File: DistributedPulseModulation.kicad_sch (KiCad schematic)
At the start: 59 parts, among them J1 Conn_02x12_Odd_Even, J2 Conn_01x01, U1 74LS251, U10 4053, U11 4053, U12 4053, U2 74LVC2G74, U25 74LS85, U28 74LS85, U31 74LS85, U4 MCP23017_SP, U7 4053, U8 4040, U9 4040

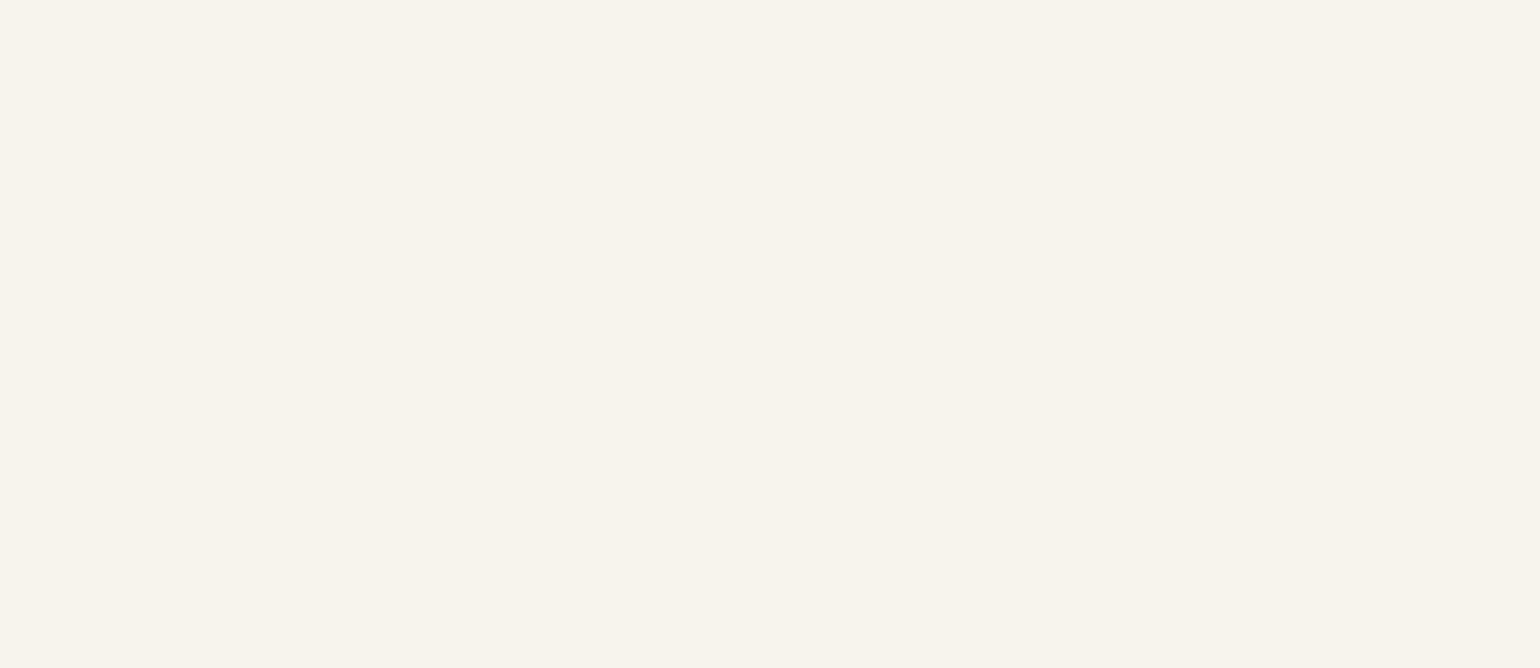
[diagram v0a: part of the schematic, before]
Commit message: [UPGRADE] : KiCad10 + Voltage -> KICAD 10 -> CMOS vs TTL voltage compare
[TODO]
-> adding replacement circuit for Dlatch chip
-> correction voltage bugs
-> remove supply voltage regulator from PCB
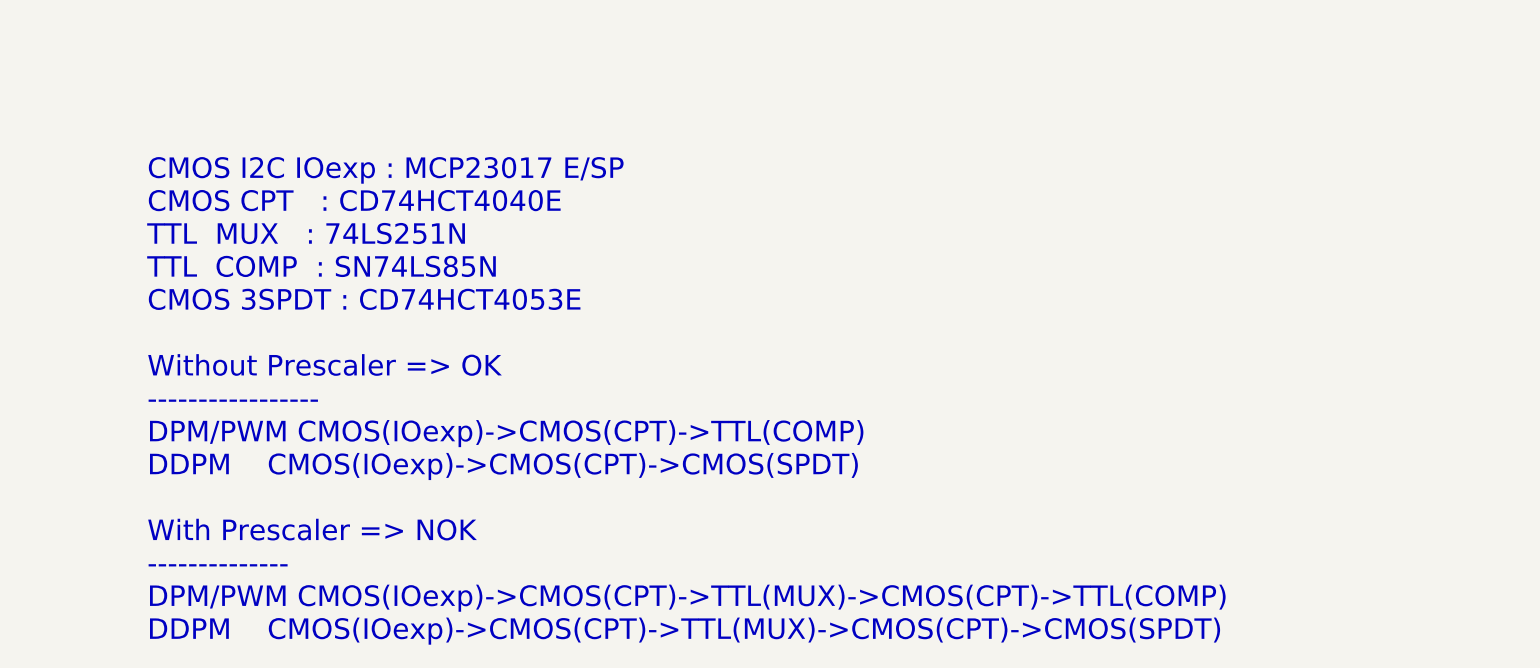
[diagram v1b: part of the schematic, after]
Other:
- note added: "CMOS I2C IOexp : MCP23017 E/SP CMOS CPT : CD74HCT4040E TTL MUX : 74LS251N TTL COMP : SN74LS85N CMOS 3SPDT : CD74HCT4053E Without Prescaler => OK ----------------- DPM/PWM CMOS(IOexp)->CMOS(CPT)->TTL(COMP) DDPM CMOS(IOexp)->CMOS(CPT)->CMOS(SPDT) With Prescaler => NOK -------------- DPM/PWM CMOS(IOexp)->CMOS(CPT)->TTL(MUX)->CMOS(CPT)->TTL(COMP) DDPM CMOS(IOexp)->CMOS(CPT)->TTL(MUX)->CMOS(CPT)->CMOS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"

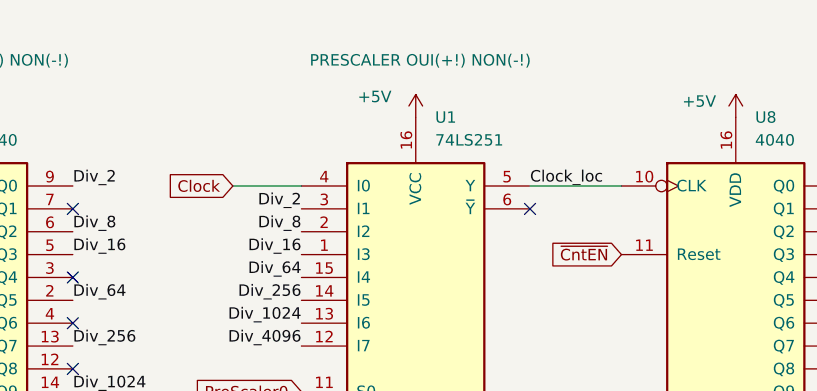
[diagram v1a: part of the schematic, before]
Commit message: [UPGRADE] : ajout R6 pour pb tension entre TTL et CMOS - A jout de R6 (2.2K) en pull-uup sur la pin 5 du 74ls251 (TTL) en entrée du 74HCT4040 (CMOS)
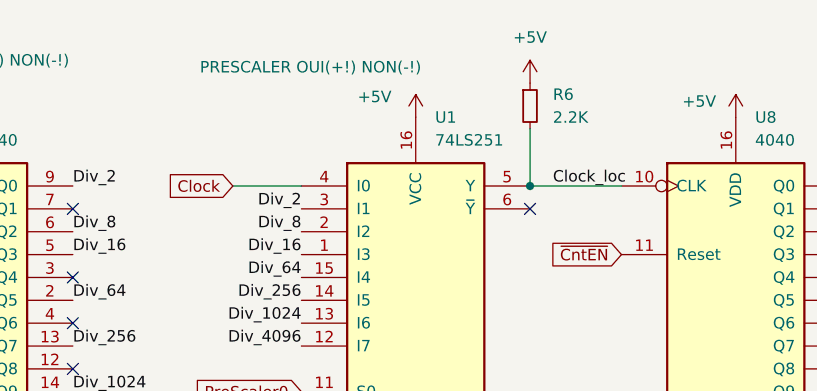
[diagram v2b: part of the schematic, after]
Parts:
- added R6: 2.2K, Resistor_SMD:R_1206_3216Metric_Pad1.30x1.75mm_HandSolder, symbol Device:R_Small
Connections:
- net +5V: now also R6.1
- net Clock_loc: now also R6.2
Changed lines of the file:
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@@
 	)
 	(junction
+		(at 105.41 36.83)
+		(diameter 0)
+		(color 0 0 0 0)
+	)
+	(junction
 		(at 212.09 260.35)
 		(diameter 0)
@@
 	(wire
 		(pts
+			(xy 105.41 30.48) (xy 105.41 36.83)
+		)
+		(stroke
+			(width 0)
+			(type default)
+		)
+	)
+	(wire
+		(pts
 			(xy 59.69 172.72) (xy 57.15 172.72)
 		)
@@
 	)
 	(label "Clock_loc"
-		(at 105.41 36.83 0)
+		(at 107.95 36.83 0)
 		(effects
 			(font
@@
 		)
 		(property "Var" "PRESCALER OUI(+!) NON(-!)"
-			(at 93.218 22.86 0)
+			(at 81.026 23.622 0)
 			(show_name no)
 			(do_not_autoplace no)
@@
 	)
 	(symbol
+		(lib_id "power:+5V")
+		(at 105.41 25.4 0)
+		(unit 1)
+		(body_style 1)
+		(exclude_from_sim no)
+		(in_bom yes)
+		(on_board yes)
+		(in_pos_files yes)
+		(dnp no)
+		(fields_autoplaced yes)
+		(property "Reference" "#PWR08"
+			(at 105.41 29.21 0)
+			(hide yes)
+			(show_name no)
+			(do_not_autoplace no)
+			(effects
+				(font
+					(size 1.27 1.27)
+				)
+			)
+		)
+		(property "Value" "+5V"
+			(at 105.41 20.32 0)
+			(show_name no)
+			(do_not_autoplace no)
+			(effects
+				(font
+					(size 1.27 1.27)
+				)
+			)
+		)
+		(property "Footprint" ""
+			(at 105.41 25.4 0)
+			(hide yes)
+			(show_name no)
+			(do_not_autoplace no)
+			(effects
+				(font
+					(size 1.27 1.27)
+				)
+			)
+		)
+		(property "Datasheet" ""
+			(at 105.41 25.4 0)
+			(hide yes)
+			(show_name no)
+			(do_not_autoplace no)
+			(effects
+				(font
+					(size 1.27 1.27)
+				)
+			)
+		)
+		(property "Description" "Power symbol creates a global label with name \"+5V\""
+			(at 105.41 25.4 0)
+			(hide yes)
+			(show_name no)
+			(do_not_autoplace no)
+			(effects
+				(font
+					(size 1.27 1.27)
+				)
+			)
+		)
+		(pin "1"
+		)
+		(instances
+			(project "DistributedPulseModulation"
+				(path "/92d35ba6-f947-4e80-8ed2-a00ad88d5264"
+					(reference "#PWR08")
+					(unit 1)
+				)
+			)
+		)
+	)
+	(symbol
 		(lib_id "74xx:74LS85")
 		(at 271.78 78.74 0)
@@
 					(unit 1)
 				)
+			)
+		)
+	)
+	(symbol
+		(lib_id "Device:R_Small")
+		(at 105.41 27.94 0)
+		(unit 1)
+		(body_style 1)
+		(exclude_from_sim no)
+		(in_bom yes)
+		(on_board yes)
+		(in_pos_files yes)
+		(dnp no)
+		(property "Reference" "R6"
+			(at 107.95 26.67 0)
+			(show_name no)
+			(do_not_autoplace no)
+			(effects
+				(font
+					(size 1.27 1.27)
+				)
+				(justify left)
+			)
+		)
+		(property "Value" "2.2K"
+			(at 107.95 29.21 0)
+			(show_name no)
+			(do_not_autoplace no)
+			(effects
+				(font
+					(size 1.27 1.27)
+				)
+				(justify left)
+			)
+		)
+		(property "Footprint" "Resistor_SMD:R_1206_3216Metric_Pad1.30x1.75mm_HandSolder"
+			(at 105.41 27.94 0)
+			(hide yes)
+			(show_name no)
+			(do_not_autoplace no)
+			(effects
+				(font
+					(size 1.27 1.27)
+				)
+			)
+		)
+		(property "Datasheet" ""
+			(at 105.41 27.94 0)
+			(hide yes)
+			(show_name no)
+			(do_not_autoplace no)
+			(effects
+				(font
+					(size 1.27 1.27)
+				)
+			)
+		)
+		(property "Description" "Resistor, small symbol"
+			(at 105.41 27.94 0)
+			(hide yes)
+			(show_name no)
+			(do_not_autoplace no)
+			(effects
+				(font
+					(size 1.27 1.27)
+				)
+			)
+		)
+		(pin "1"
+		)
+		(pin "2"
+		)
+		(instances
+			(project "DistributedPulseModulation"
+				(path "/92d35ba6-f947-4e80-8ed2-a00ad88d5264"
+					(reference "R6")
+					(unit 1)
+				)

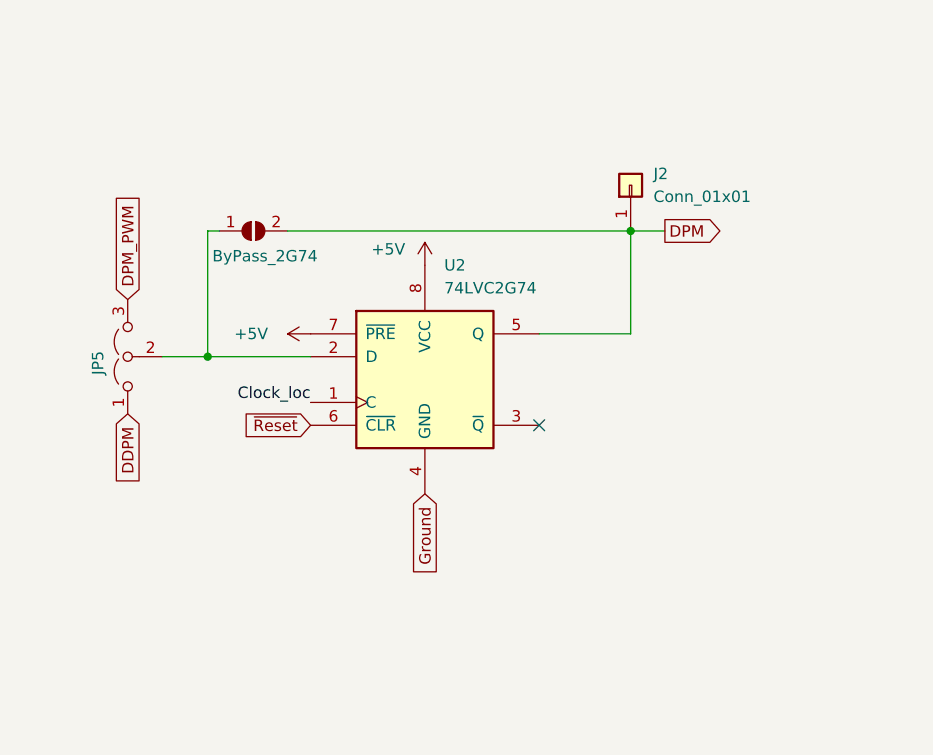
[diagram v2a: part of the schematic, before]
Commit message: [UPGRADE] : ajout R7 pour pb tension entre TTL et CMOS - A jout de R7 (2.2K) en pull-up sur la sortie finale de la carte
[TODO]
-> adding replacement circuit for Dlatch chip
-> remove supply voltage regulator from PCB

[DONE]
-> correction voltage bugs
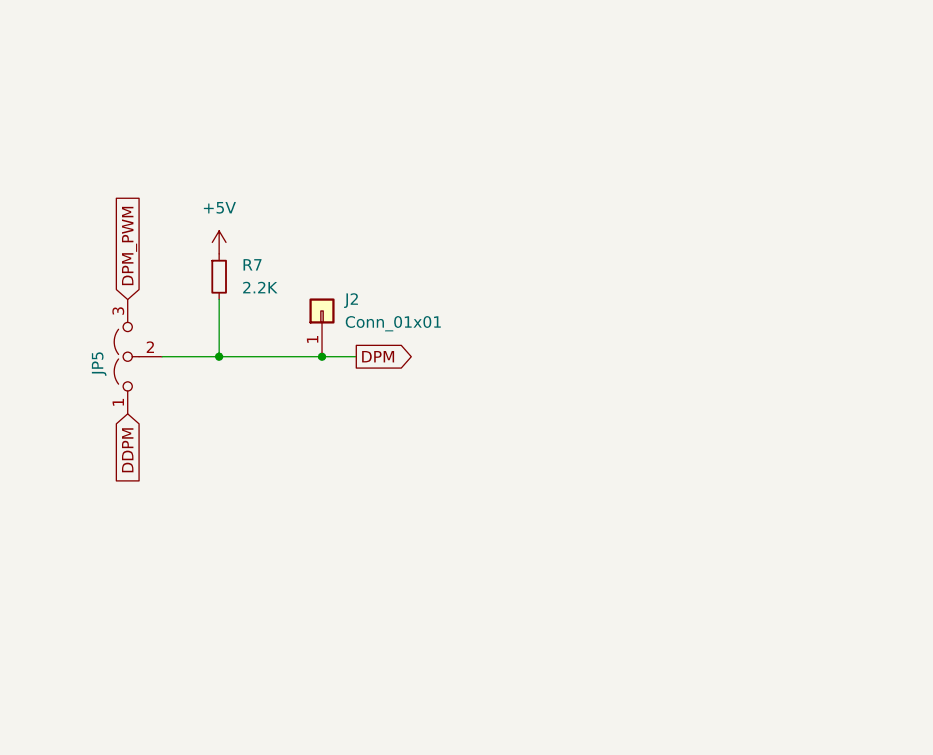
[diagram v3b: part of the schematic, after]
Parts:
- removed ByPass_2G74: SolderJumper_2_Open, Jumper:SolderJumper-2_P1.3mm_Open_TrianglePad1.0x1.5mm, symbol Jumper:SolderJumper_2_Open
- removed U2: 74LVC2G74, Package_SO:SSOP-8_2.95x2.8mm_P0.65mm, symbol 74xGxx:74LVC2G74
- added R7: 2.2K, Resistor_SMD:R_1206_3216Metric_Pad1.30x1.75mm_HandSolder, symbol Device:R_Small
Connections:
- net +5V: now also R7.1
- net DPM: now also JP5.2 (C), R7.2
- no-connect marks 26 -> 25
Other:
- moved on the sheet: J2
